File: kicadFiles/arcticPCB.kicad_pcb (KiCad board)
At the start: 2 copper layers, 283 x 94.2 mm, 175 parts, among them J1 TYPE-C-31-M12_13, J2 Conn_01x14, J3 Conn_ARM_JTAG_SWD_10, SW1 ESC, SW10 0, SW11 -_, SW12 =+, SW13 LBKSP, SW14 2U BKSP, SW15 TAB_150, SW16 Q, SW17 W, SW18 E, SW19 R, SW2 1, SW20 T, SW21 Y, SW22 U, SW23 I, SW24 O, SW25 P, SW26 [{, SW27 ]}, SW28 \|_150, SW29 CAPS_175, SW3 2, SW30 A, SW31 S, SW32 D, SW33 F, SW34 G, SW35 H, SW36 J, SW37 K, SW38 L, SW39 :;, SW4 3, SW40 "', SW41 ENTER_225, SW42 LSHIFT_225, SW43 Z, SW44 X, SW45 C, SW46 V, SW47 B, SW48 N, SW49 M, SW5 4, SW50 <,, SW51 >., SW52 ?/, SW53 RSHIFT_275, SW54 LCTRL_150, SW55 LGUI_100, SW56 LALT_150, SW57 SPACE_7U, SW58 RALT_150, SW59 RGUI_100, SW6 5, SW60 RCTRL_150, SW61 FN_100, SW62 RSHIFT_175, SW63 STEPPED_CAPS_125, SW64 1U LBKSP, SW65 1U RBKSP, SW7 7, SW8 8, SW9 9, U1 STM32F072-LQFP48, U2 USBLC6-2SC6, U3 MCP1700-3302E_SOT23

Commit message: Fiz RShift / Enter stab collision issue
- The RShift and Enter stabs were positioned in a way that they would collide. The Enter stab was rotated to avoid this.
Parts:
- SW10: value 0 -> 9
- SW11: value -_ -> 0
- SW12: value =+ -> -_
- SW13: value LBKSP -> +=
- SW41: footprint acheron_MX_SolderMask:MX225 -> acheron_MX_SolderMask:MX225R
- SW7: value 7 -> 6
- SW8: value 8 -> 7
- SW9: value 9 -> 8
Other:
- net class Default: clearance 0.127 -> 0.1524
- rule trace_clearance: 0.127 -> 0.1524

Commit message: Solve pre-Alpha prototype issues
This commit solves the issues found in the pre-Alpha prototypes:

- In the USB connector, the D+ and D- pads were switched; this has been fixed and the differential pair routing was improved;
- The split Right Shift keyswitches SW62 for the 1.75U RShift and 1U SW61 for the Fn were in the wrong orientation: the Fn key SW61 was on the left and SW62 was on the left. They were swapped for the right orientation now;
- Also, to make firmware definitions easier, the 1.75U RShift key and 2.75U RShift key are now at the same position, whereas in pre-Alpha SW62 for the 1.75RShift was at the same position with SW61 for the 1U Fn, which made firmware need two definitions. This has now been fixed.
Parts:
- moved D53 33.3 mm to (89.0, 142.6)
- moved SW61 33.3 mm to (79.5, 148.5)
- moved D62 27.4 mm to (116.4, 142.6)
- moved SW62 19.1 mm to (105.7, 148.5)
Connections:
- J1 pad A6: DBus- -> DBus+
- J1 pad A7: DBus+ -> DBus-
- J1 pad B6: DBus- -> DBus+
- J1 pad B7: DBus+ -> DBus-
- SW53 pad 2: Net-(D53-Pad2) -> Net-(D62-Pad2)
- SW61 pad 1: Col12 -> Col13
- SW62 pad 1: Col13 -> Col12
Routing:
- net Net-(D53-Pad2): track 23.3 -> 6.45 mm
- net Net-(D62-Pad2): track 3.61 -> 17.2 mm
- net NRST: track 88.1 -> 100.2 mm
- net D+: track 65.3 -> 55.8 mm
- net Col12: track 373.2 -> 369.6 mm
- net Col1: track 182.3 -> 184.2 mm
- net Col13: track 328.4 -> 330.0 mm
- net DBus-: track 15.8 -> 16.9 mm
- net DBus+: track 15.8 -> 14.7 mm, vias 0 -> 2
- net D-: track 56.8 -> 55.9 mm
- net Col11: track 392.3 -> 391.6 mm
- net Row4: track 272.5 -> 271.8 mm
- net GND: vias 2 -> 3
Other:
- net class Default: clearance 0.1524 -> 0.127
- rule trace_clearance: 0.1524 -> 0.127

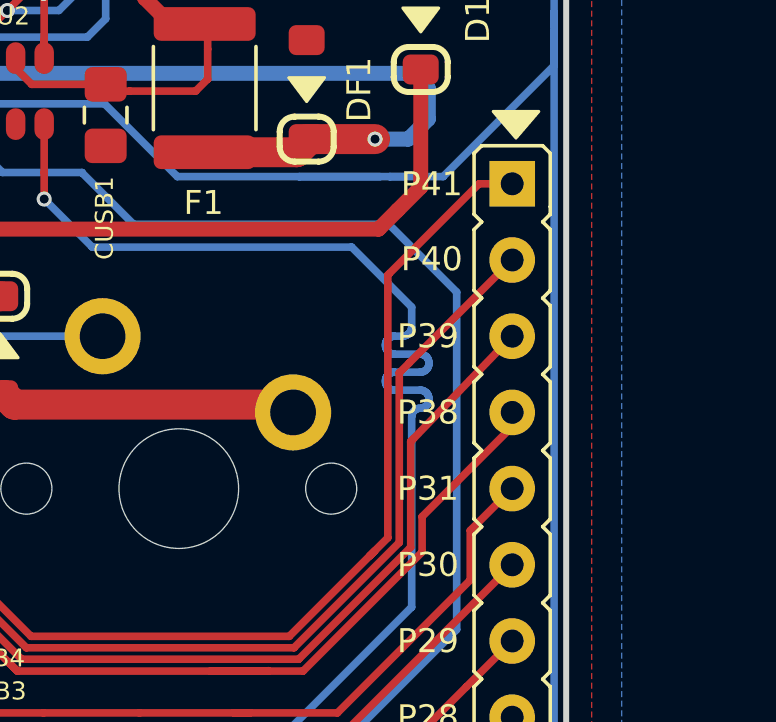
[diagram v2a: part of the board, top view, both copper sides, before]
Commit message: Refresh renders for rev Alpha
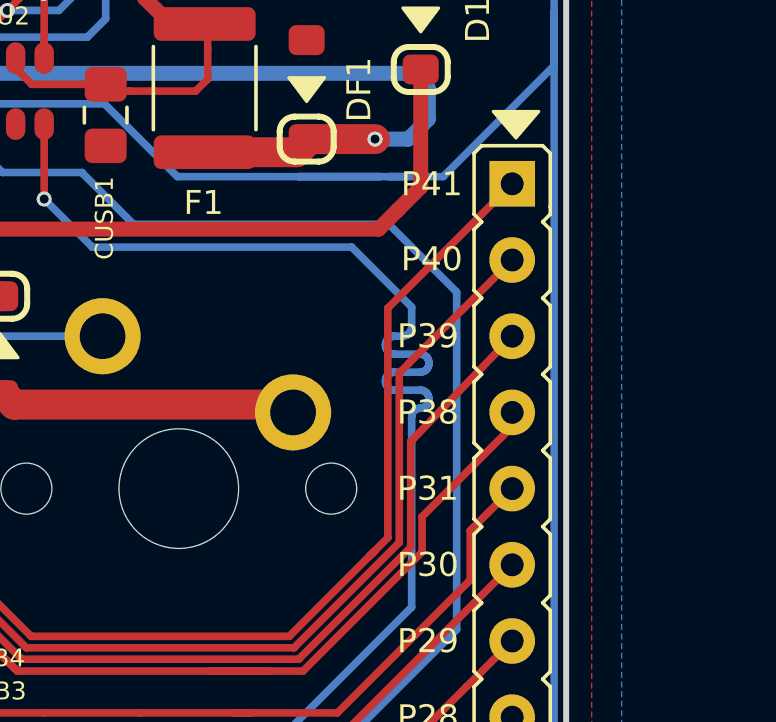
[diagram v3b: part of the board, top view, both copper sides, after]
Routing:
- net Extra1: track 38.5 -> 37.8 mm
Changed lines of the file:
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@@
     (thickness 1.6)
     (drawings 128)
-    (tracks 1409)
+    (tracks 1407)
     (modules 175)
     (nets 119)
@@
       (drillshape 0)
       (scaleselection 1)
-      (outputdirectory "../arcticGerbers")
+      (outputdirectory "../alpha/gerbers")
     )
   )
@@
   (segment (start 338.47625 88.678125) (end 338.47625 91.803125) (width 0.254) (layer "F.Cu") (net 87))
   (segment (start 337.47625 88.678125) (end 337.47625 91.053125) (width 0.254) (layer "F.Cu") (net 87))
-  (segment (start 348.41825 103.247125) (end 351.42225 100.243125) (width 0.254) (layer "F.Cu") (net 115))
-  (segment (start 348.381443 112.042448) (end 348.381443 103.283932) (width 0.254) (layer "F.Cu") (net 115))
-  (segment (start 348.381443 103.283932) (end 348.41825 103.247125) (width 0.254) (layer "F.Cu") (net 115))
   (segment (start 347.95423 112.469661) (end 347.781008 112.642883) (width 0.254) (layer "F.Cu") (net 115))
   (segment (start 347.781008 112.642883) (end 345.09643 115.327461) (width 0.254) (layer "F.Cu") (net 115))
-  (segment (start 347.781008 112.642883) (end 348.381443 112.042448) (width 0.254) (layer "F.Cu") (net 115))
   (segment (start 336.489414 115.327461) (end 334.715078 113.553125) (width 0.254) (layer "F.Cu") (net 115))
   (segment (start 334.715078 113.553125) (end 329.134806 113.553125) (width 0.254) (layer "F.Cu") (net 115))
@@
   (segment (start 329.134806 113.553125) (end 327.87617 114.811761) (width 0.254) (layer "F.Cu") (net 115))
   (segment (start 327.87617 114.811761) (end 327.87617 115.765745) (width 0.254) (layer "F.Cu") (net 115))
-  (segment (start 351.42225 100.243125) (end 352.52625 100.243125) (width 0.254) (layer "F.Cu") (net 115))
   (segment (start 348.762453 112.200266) (end 348.762453 106.546922) (width 0.254) (layer "F.Cu") (net 114))
   (segment (start 345.254248 115.708471) (end 348.762453 112.200266) (width 0.254) (layer "F.Cu") (net 114))
@@
   (segment (start 316.84176 150.643995) (end 315.67625 151.809505) (width 0.5) (layer "F.Cu") (net 1))
   (segment (start 315.87924 146.593995) (end 315.87924 152.353125) (width 0.5) (layer "F.Cu") (net 1))
+  (segment (start 348.381443 112.042448) (end 348.381443 104.387932) (width 0.254) (layer "F.Cu") (net 115))
+  (segment (start 348.381443 104.387932) (end 352.52625 100.243125) (width 0.254) (layer "F.Cu") (net 115))
+  (segment (start 347.781008 112.642883) (end 348.381443 112.042448) (width 0.254) (layer "F.Cu") (net 115))
   (zone (net 0) (net_name "") (layer "F.Cu") (hatch edge 0.508)
     (connect_pads (clearance 0.508))

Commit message: Updated files and README
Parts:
- added L6: Putain Logo, arcticGraphics:putainLogo_50_5, F.Cu at (250.9, 117.1)
- moved L3 53.6 mm to (155.7, 117.4)
